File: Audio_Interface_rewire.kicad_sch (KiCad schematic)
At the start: 62 parts, among them IC1 REG103GA-3.3_2K5, IC2 PCM2906CDB, IC3 INA849DGKT, J1 USB_B_Micro, J2 SJ-435107RS, J3 Vol. knob1 22k, J4 Vol. knob2 22k, J5 External Mic Conn., Q1 J304, SW1 HID0, SW2 HID1, SW3 HID2, SW4 SW_Push_DPDT, U1 NMA0515SC, Y1 12MHz

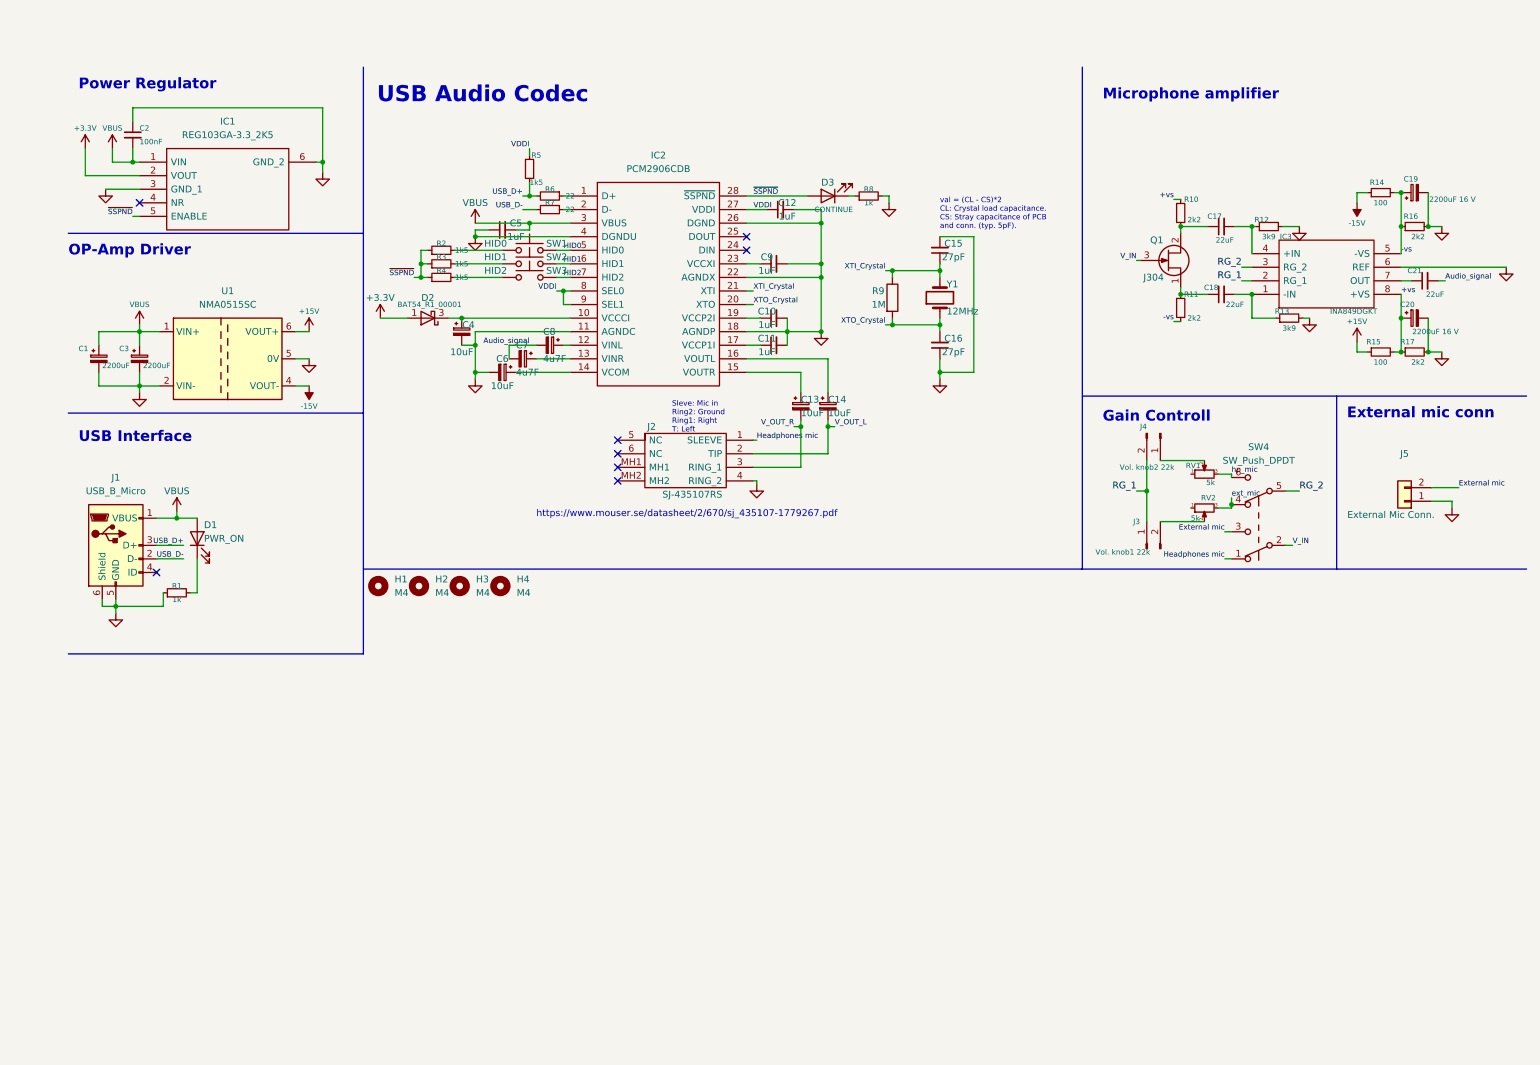
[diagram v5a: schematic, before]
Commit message: Changed microphone input system
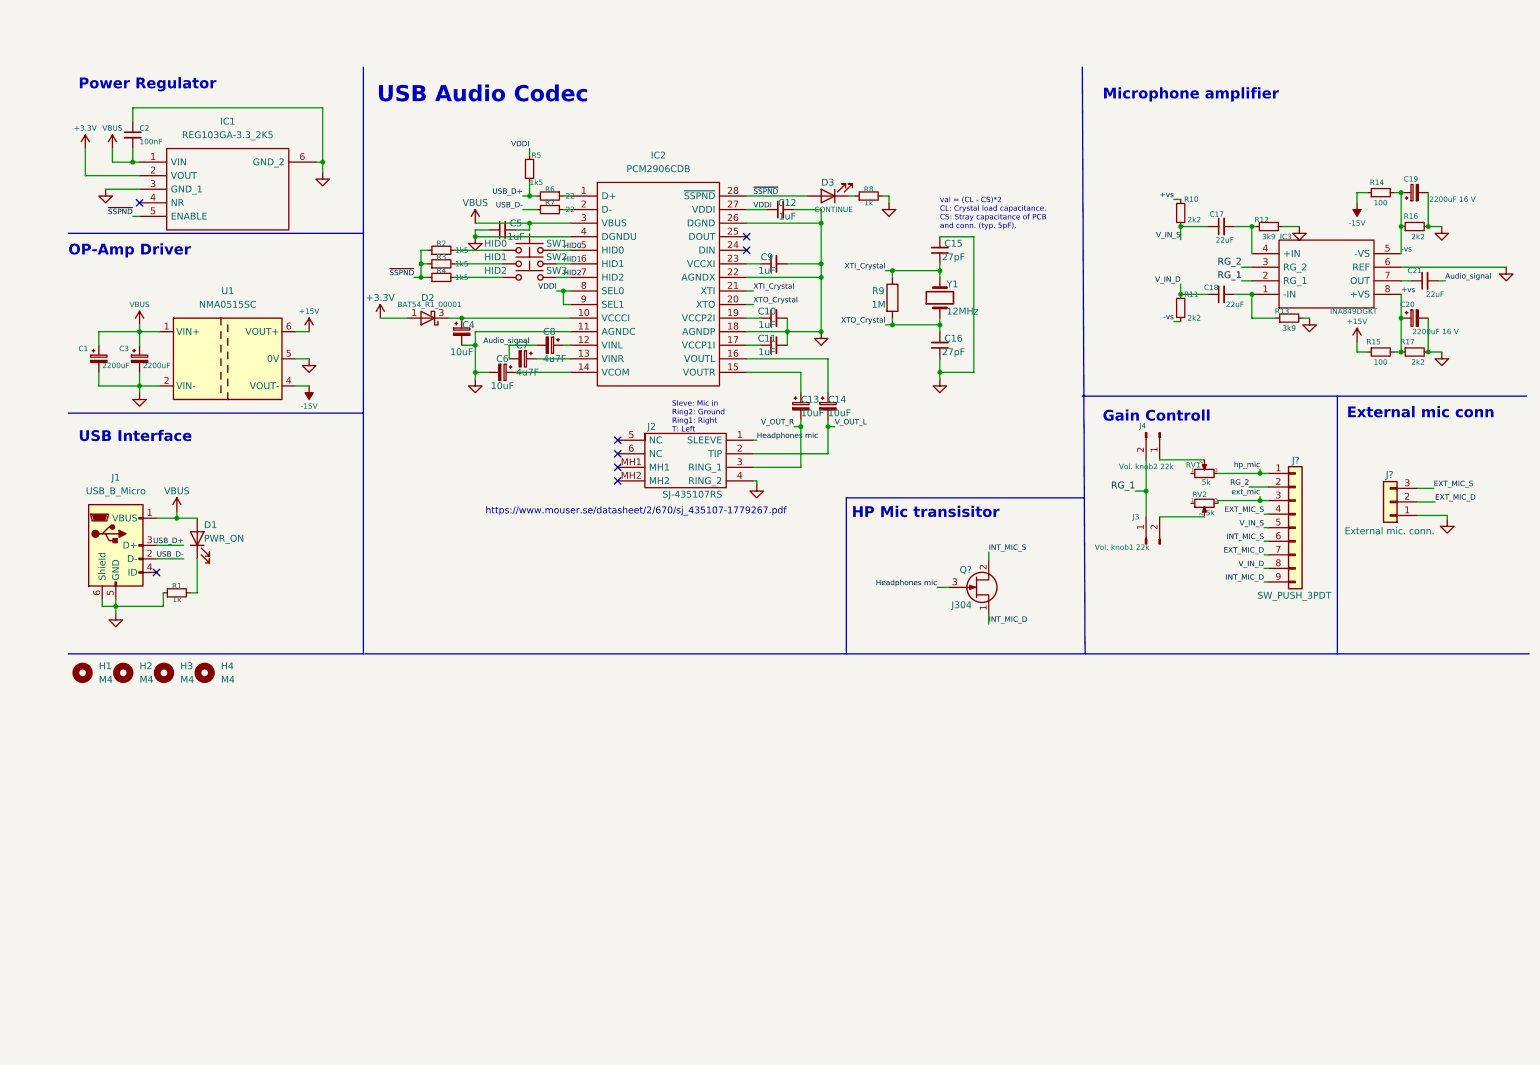
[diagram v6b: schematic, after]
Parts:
- removed J5: External Mic Conn., Connector_JST:JST_XH_B2B-XH-AM_1x02_P2.50mm_Vertical, symbol Connector_Generic:Conn_01x02
- removed Q1: J304, Package_TO_SOT_SMD:SOT-23, symbol Transistor_FET:BF545B
- removed SW4: SW_Push_DPDT, Connector_JST:JST_XH_B6B-XH-AM_1x06_P2.50mm_Vertical, symbol Switch:SW_Push_DPDT
- added J?: External mic. conn., symbol Connector_Generic:Conn_01x03
- added J?: SW_PUSH_3PDT, symbol Connector_Generic:Conn_01x09
- added Q?: J304, Package_TO_SOT_SMD:SOT-23, symbol Transistor_FET:BF545B
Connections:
- net GND: now also J?.1 (Pin_1)
- net Headphones mic: now also Q?.3 (G)
- net RG_2: now also J?.2 (Pin_2)
- net ext_mic: now also J?.3 (Pin_3)
- net hp_mic: now also J?.1 (Pin_1)
- net V_IN_D: now reaches C18.1, R11.1
- net V_IN_D: now also J?.8 (Pin_8)
- net V_IN_S: now reaches C17.1, R10.2
- net V_IN_S: now also J?.5 (Pin_5)
- new net EXT_MIC_D: J?.2 (Pin_2), J?.7 (Pin_7)
- new net EXT_MIC_S: J?.3 (Pin_3), J?.4 (Pin_4)
- new net INT_MIC_D: J?.9 (Pin_9), Q?.1 (S)
- new net INT_MIC_S: J?.6 (Pin_6), Q?.2 (D)
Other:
- note added: "HP Mic transisitor"
- moved on the sheet: H1, H2, H3, H4, J3, RV2

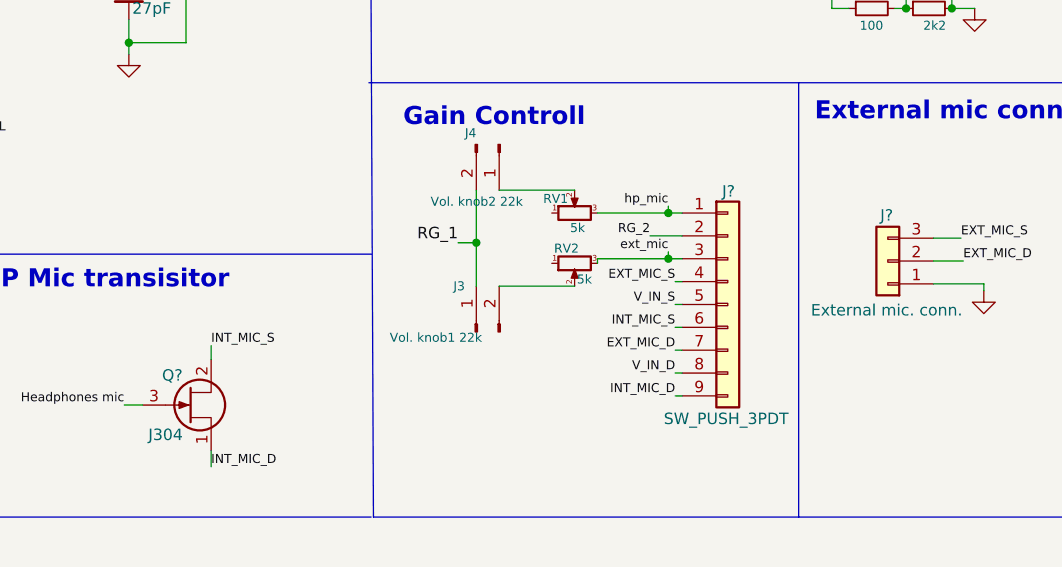
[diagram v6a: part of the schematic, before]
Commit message: started wiring the pcb
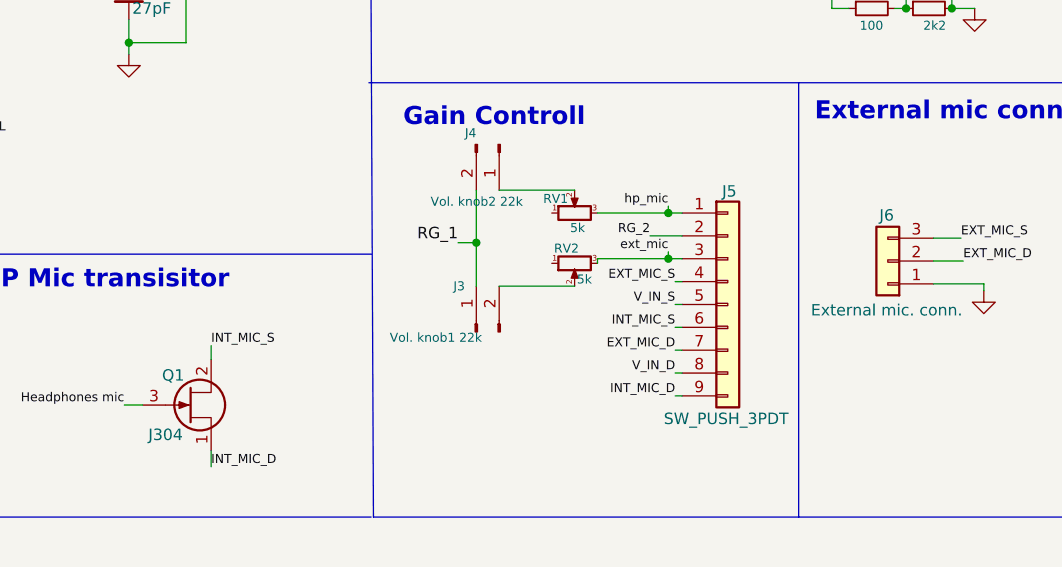
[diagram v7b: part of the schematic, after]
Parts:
- C4: footprint Capacitor_THT:CP_Radial_D8.0mm_P5.00mm -> Capacitor_SMD:C_0805_2012Metric_Pad1.18x1.45mm_HandSolder
- IC2: footprint Package_SO:SOP65P780X200-28N -> IC_Downloaded:SOP65P780X200-28N
- J5: renamed from J?; footprint (none) -> Connector_JST:JST_XH_B9B-XH-AM_1x09_P2.50mm_Vertical
- J6: renamed from J?; footprint (none) -> Connector_JST:JST_XH_B3B-XH-AM_1x03_P2.50mm_Vertical
- gave numbers to parts that had none: 1
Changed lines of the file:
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@@
   (symbol (lib_id "Connector_Generic:Conn_01x03") (at 259.588 93.472 180) (unit 1)
     (in_bom yes) (on_board yes)
-    (property "Reference" "J?" (id 0) (at 259.461 88.392 0))
+    (property "Reference" "J6" (id 0) (at 259.461 88.392 0))
     (property "Value" "External mic. conn." (id 1) (at 259.461 98.933 0))
-    (property "Footprint" "" (id 2) (at 259.588 93.472 0)
+    (property "Footprint" "Connector_JST:JST_XH_B3B-XH-AM_1x03_P2.50mm_Vertical" (id 2) (at 259.588 93.472 0)
       (effects (font (size 1.27 1.27)) hide)
     )
@@
   (symbol (lib_id "Connector_Generic:Conn_01x09") (at 241.808 98.298 0) (unit 1)
     (in_bom yes) (on_board yes)
-    (property "Reference" "J?" (id 0) (at 241.173 85.725 0)
+    (property "Reference" "J5" (id 0) (at 241.173 85.725 0)
       (effects (font (size 1.27 1.27)) (justify left))
     )
@@
       (effects (font (size 1.27 1.27)) (justify left))
     )
-    (property "Footprint" "" (id 2) (at 241.808 98.298 0)
+    (property "Footprint" "Connector_JST:JST_XH_B9B-XH-AM_1x09_P2.50mm_Vertical" (id 2) (at 241.808 98.298 0)
       (effects (font (size 1.27 1.27)) hide)
     )
@@
     (property "Reference" "IC2" (id 0) (at 122.555 28.575 0))
     (property "Value" "PCM2906CDB" (id 1) (at 122.555 31.115 0))
-    (property "Footprint" "Package_SO:SOP65P780X200-28N" (id 2) (at 98.425 84.455 0)
+    (property "Footprint" "IC_Downloaded:SOP65P780X200-28N" (id 2) (at 98.425 84.455 0)
       (effects (font (size 1.27 1.27)) (justify left) hide)
     )
@@
   (symbol (lib_id "Transistor_FET:BF545B") (at 181.864 109.474 0) (unit 1)
     (in_bom yes) (on_board yes)
-    (property "Reference" "Q?" (id 0) (at 178.943 106.172 0)
+    (property "Reference" "Q1" (id 0) (at 178.943 106.172 0)
       (effects (font (size 1.27 1.27)) (justify left))
     )
@@
     (property "Reference" "C4" (id 0) (at 86.995 60.325 0))
     (property "Value" "10uF" (id 1) (at 85.725 65.405 0))
-    (property "Footprint" "Capacitor_THT:CP_Radial_D8.0mm_P5.00mm" (id 2) (at 85.725 61.595 0)
+    (property "Footprint" "Capacitor_SMD:C_0805_2012Metric_Pad1.18x1.45mm_HandSolder" (id 2) (at 85.725 61.595 0)
       (effects (font (size 1.27 1.27)) hide)
     )
@@
     )
     (path "/5d317a70-638c-4b9a-a3aa-1168c8039fe5"
-      (reference "C4") (unit 1) (value "10uF") (footprint "Capacitor_THT:CP_Radial_D8.0mm_P5.00mm")
+      (reference "C4") (unit 1) (value "10uF") (footprint "Capacitor_SMD:C_0805_2012Metric_Pad1.18x1.45mm_HandSolder")
     )
     (path "/6ebfa7eb-bedd-4b70-9303-703f80c384c7"
@@
     )
     (path "/129f10a1-91c5-4162-926d-17f11fb6da46"
-      (reference "IC2") (unit 1) (value "PCM2906CDB") (footprint "Package_SO:SOP65P780X200-28N")
+      (reference "IC2") (unit 1) (value "PCM2906CDB") (footprint "IC_Downloaded:SOP65P780X200-28N")
     )
     (path "/fd99694c-3df7-468b-9a79-959510cff011"
@@
       (reference "J4") (unit 1) (value "Vol. knob2 22k") (footprint "Connector_JST:JST_XH_B2B-XH-AM_1x02_P2.50mm_Vertical")
     )
+    (path "/0da21d48-c73b-400b-8aad-1e22db8c7525"
+      (reference "J5") (unit 1) (value "SW_PUSH_3PDT") (footprint "Connector_JST:JST_XH_B9B-XH-AM_1x09_P2.50mm_Vertical")
+    )
     (path "/05ac07f1-e36a-4618-bf57-aaa49072b5fd"
-      (reference "J?") (unit 1) (value "External mic. conn.") (footprint "")
-    )
-    (path "/0da21d48-c73b-400b-8aad-1e22db8c7525"
-      (reference "J?") (unit 1) (value "SW_PUSH_3PDT") (footprint "")
+      (reference "J6") (unit 1) (value "External mic. conn.") (footprint "Connector_JST:JST_XH_B3B-XH-AM_1x03_P2.50mm_Vertical")
     )
     (path "/1d7f83df-1011-45c6-91df-ca070dd19e37"
-      (reference "Q?") (unit 1) (value "J304") (footprint "Package_TO_SOT_SMD:SOT-23")
+      (reference "Q1") (unit 1) (value "J304") (footprint "Package_TO_SOT_SMD:SOT-23")
     )
     (path "/f55854b8-4a94-40db-8de4-7fe820a71876"

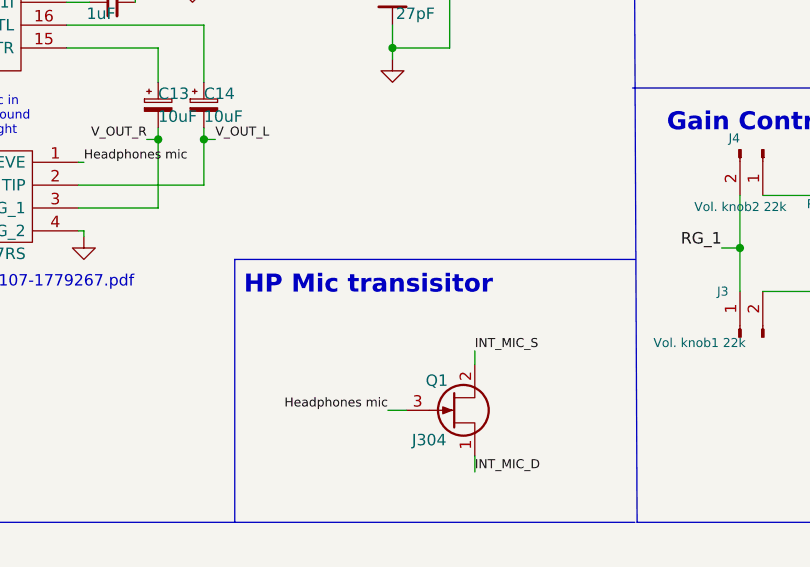
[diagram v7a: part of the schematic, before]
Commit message: Finished pcb layout for version 2.0
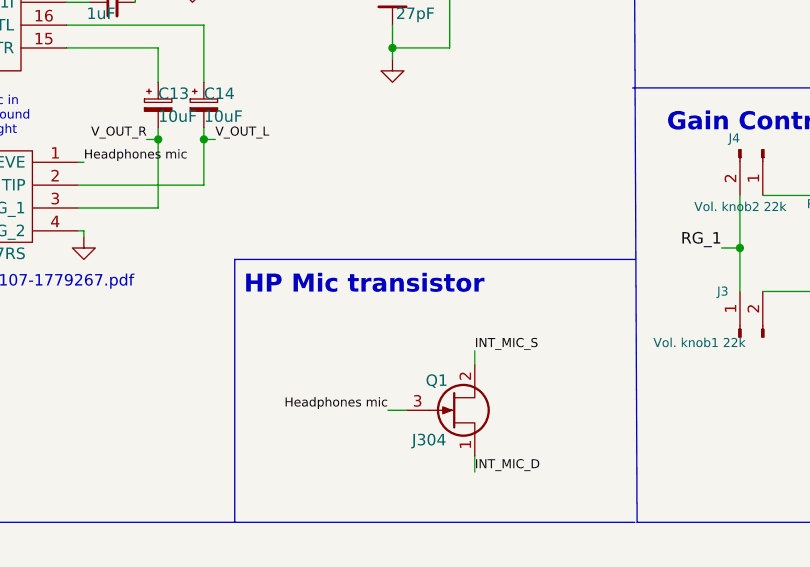
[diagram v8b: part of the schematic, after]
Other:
- note added: "HP Mic transistor"
- note removed: "HP Mic transisitor"
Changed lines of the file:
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@@
     (effects (font (size 2 2) (thickness 0.4) bold) (justify left bottom))
   )
-  (text "HP Mic transisitor" (at 158.75 96.774 0)
+  (text "HP Mic transistor" (at 158.75 96.774 0)
     (effects (font (size 2 2) (thickness 0.4) bold) (justify left bottom))
   )
